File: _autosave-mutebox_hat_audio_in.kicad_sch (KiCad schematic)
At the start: 49 parts, among them J1 GPIO, J3 RCJ-042, J4 RCJ-042, U2 74LVC157, U3 PCM1862DBT, Y3 XO1

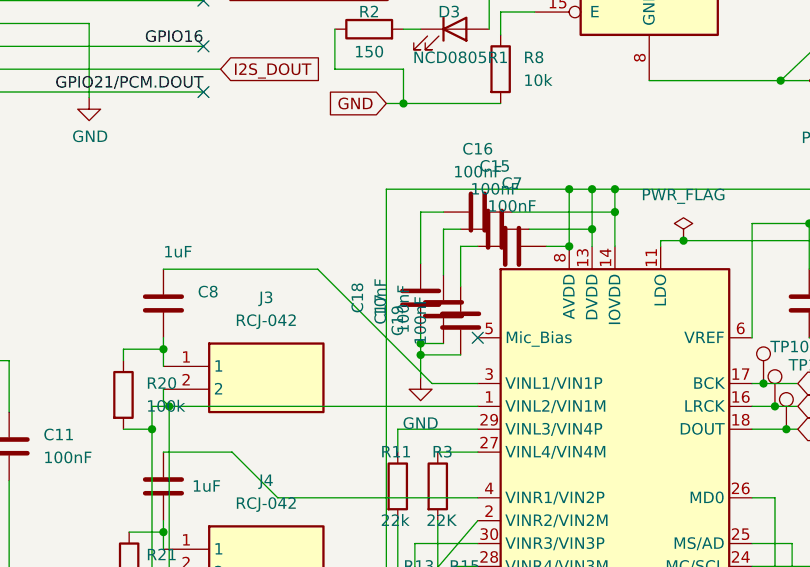
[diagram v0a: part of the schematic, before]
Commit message: Cleaned up a lot around the PCM1862.  ADC side looking pretty good
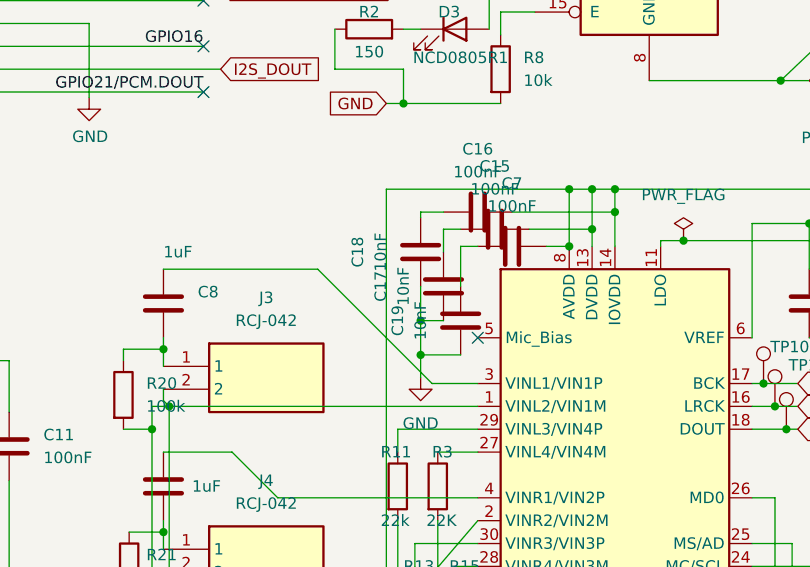
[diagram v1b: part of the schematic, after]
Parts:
- C15, C16, C7: footprint (none) -> Capacitor_SMD:C_0402_1005Metric
- C17, C19: value 100nF -> 10nF; footprint (none) -> Capacitor_SMD:C_0402_1005Metric; LCSC C1525 -> C15195
- C18: footprint (none) -> Capacitor_SMD:C_0402_1005Metric; LCSC C1525 -> C15195
- D3: footprint LED_SMD:LED_0805_2012Metric_Pad1.15x1.40mm_HandSolder -> Capacitor_SMD:C_0402_1005Metric
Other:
- moved on the sheet: C17, C18
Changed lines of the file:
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@@
 	)
 	(junction
-		(at 124.46 104.14)
-		(diameter 0)
-		(color 0 0 0 0)
-	)
-	(junction
 		(at 96.52 160.655)
 		(diameter 0)
@@
 	)
 	(junction
+		(at 124.46 101.6)
+		(diameter 0)
+		(color 0 0 0 0)
+	)
+	(junction
 		(at 76.2 43.18)
 		(diameter 1.016)
@@
 	(wire
 		(pts
-			(xy 127 91.44) (xy 127 96.52)
+			(xy 127 91.44) (xy 127 93.98)
 		)
 		(stroke
@@
 	(wire
 		(pts
-			(xy 124.46 104.14) (xy 127 104.14)
+			(xy 124.46 101.6) (xy 127 101.6)
 		)
 		(stroke
@@
 	(wire
 		(pts
-			(xy 124.46 89.535) (xy 124.46 95.25)
+			(xy 124.46 89.535) (xy 124.46 90.17)
 		)
 		(stroke
@@
 	(wire
 		(pts
-			(xy 124.46 102.87) (xy 124.46 104.14)
+			(xy 124.46 97.79) (xy 124.46 101.6)
 		)
 		(stroke
@@
 	(wire
 		(pts
+			(xy 124.46 101.6) (xy 124.46 105.41)
+		)
+		(stroke
+			(width 0)
+			(type default)
+		)
+	)
+	(wire
+		(pts
 			(xy 33.02 105.41) (xy 36.83 105.41)
 		)
@@
 	(wire
 		(pts
-			(xy 124.46 104.14) (xy 124.46 105.41)
-		)
-		(stroke
-			(width 0)
-			(type default)
-		)
-	)
-	(wire
-		(pts
 			(xy 136.525 91.44) (xy 143.51 91.44)
 		)
@@
 			)
 		)
-		(property "Footprint" "LED_SMD:LED_0805_2012Metric_Pad1.15x1.40mm_HandSolder"
+		(property "Footprint" "Capacitor_SMD:C_0402_1005Metric"
 			(at 128.27 69.215 0)
 			(effects
@@
 			)
 		)
-		(property "Value" "100nF"
+		(property "Value" "10nF"
 			(at 124.46 101.6 90)
 			(effects
@@
 			)
 		)
-		(property "Footprint" ""
+		(property "Footprint" "Capacitor_SMD:C_0402_1005Metric"
 			(at 127.9398 105.41 0)
 			(effects
@@
 			)
 		)
-		(property "LCSC" "C1525"
+		(property "LCSC" "C15195"
 			(at 128.905 101.6 90)
 			(effects
@@
 			)
 		)
-		(property "Footprint" ""
+		(property "Footprint" "Capacitor_SMD:C_0402_1005Metric"
 			(at 134.62 88.5698 0)
 			(effects
@@
 			)
 		)
-		(property "Footprint" ""
+		(property "Footprint" "Capacitor_SMD:C_0402_1005Metric"
 			(at 138.43 92.3798 0)
 			(effects
@@
 	(symbol
 		(lib_id "Device:C")
-		(at 124.46 99.06 0)
+		(at 124.46 93.98 0)
 		(mirror y)
 		(unit 1)
@@
 		(dnp no)
 		(property "Reference" "C18"
-			(at 117.475 99.06 90)
+			(at 117.475 93.98 90)
 			(effects
 				(font
@@
 		)
 		(property "Value" "10nF"
-			(at 120.015 99.06 90)
+			(at 120.015 93.98 90)
 			(effects
 				(font
@@
 			)
 		)
-		(property "Footprint" ""
-			(at 123.4948 102.87 0)
+		(property "Footprint" "Capacitor_SMD:C_0402_1005Metric"
+			(at 123.4948 97.79 0)
 			(effects
 				(font
@@
 		)
 		(property "Datasheet" "~"
-			(at 124.46 99.06 0)
+			(at 124.46 93.98 0)
 			(effects
 				(font
@@
 		)
 		(property "Description" "Unpolarized capacitor"
-			(at 124.46 99.06 0)
+			(at 124.46 93.98 0)
 			(effects
 				(font
@@
 			)
 		)
-		(property "LCSC" "C1525"
-			(at 124.46 99.06 90)
+		(property "LCSC" "C15195"
+			(at 124.46 93.98 90)
 			(effects
 				(font
@@
 			)
 		)
-		(property "Footprint" ""
+		(property "Footprint" "Capacitor_SMD:C_0402_1005Metric"
 			(at 136.525 90.4748 0)
 			(effects
@@
 	(symbol
 		(lib_id "Device:C")
-		(at 127 100.33 0)
+		(at 127 97.79 0)
 		(mirror y)
 		(unit 1)
@@
 		(dnp no)
 		(property "Reference" "C17"
-			(at 120.015 100.33 90)
+			(at 120.015 97.79 90)
 			(effects
 				(font
@@
 			)
 		)
-		(property "Value" "100nF"
-			(at 122.555 100.33 90)
+		(property "Value" "10nF"
+			(at 122.555 97.79 90)
 			(effects
 				(font
@@
 			)
 		)
-		(property "Footprint" ""
-			(at 126.0348 104.14 0)
+		(property "Footprint" "Capacitor_SMD:C_0402_1005Metric"
+			(at 126.0348 101.6 0)
 			(effects
 				(font
@@
 		)
 		(property "Datasheet" "~"
-			(at 127 100.33 0)
+			(at 127 97.79 0)
 			(effects
 				(font
@@
 		)
 		(property "Description" "Unpolarized capacitor"
-			(at 127 100.33 0)
+			(at 127 97.79 0)
 			(effects
 				(font
@@
 			)
 		)
-		(property "LCSC" "C1525"
-			(at 127 100.33 90)
+		(property "LCSC" "C15195"
+			(at 127 97.79 90)
 			(effects
 				(font
